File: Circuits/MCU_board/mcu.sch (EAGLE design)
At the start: 78 parts, among them IC1 RP111N331B-TR-FE, IC2 FT230XS, U1 TCA9548APWR, U2 USBLC6-2P6, U4 LSM9DS1, U5 STM32L452RECT6

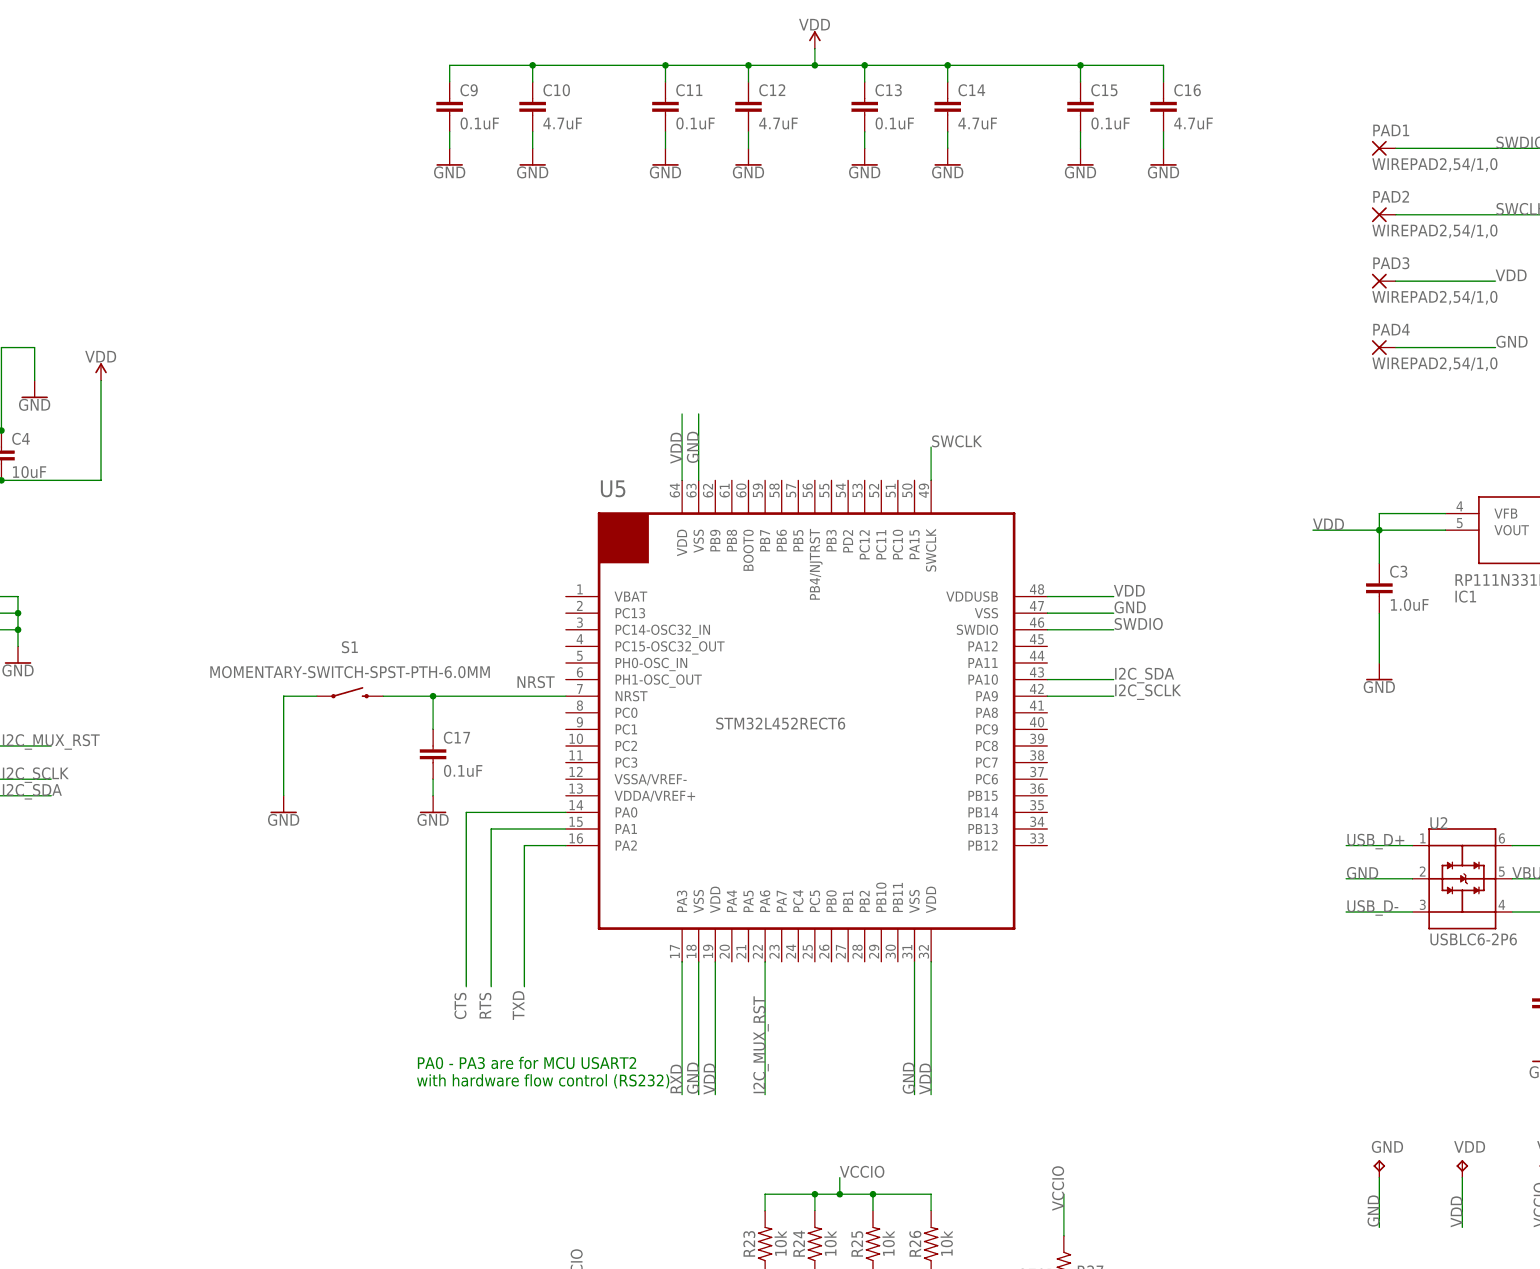
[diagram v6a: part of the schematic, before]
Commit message: Iteration 2 of MCU board * Change decoupling caps * Power all VDD and VSS pins * Add LED to GPIO * Add Pullup to USB D+ * Add jumpers for BOOT0
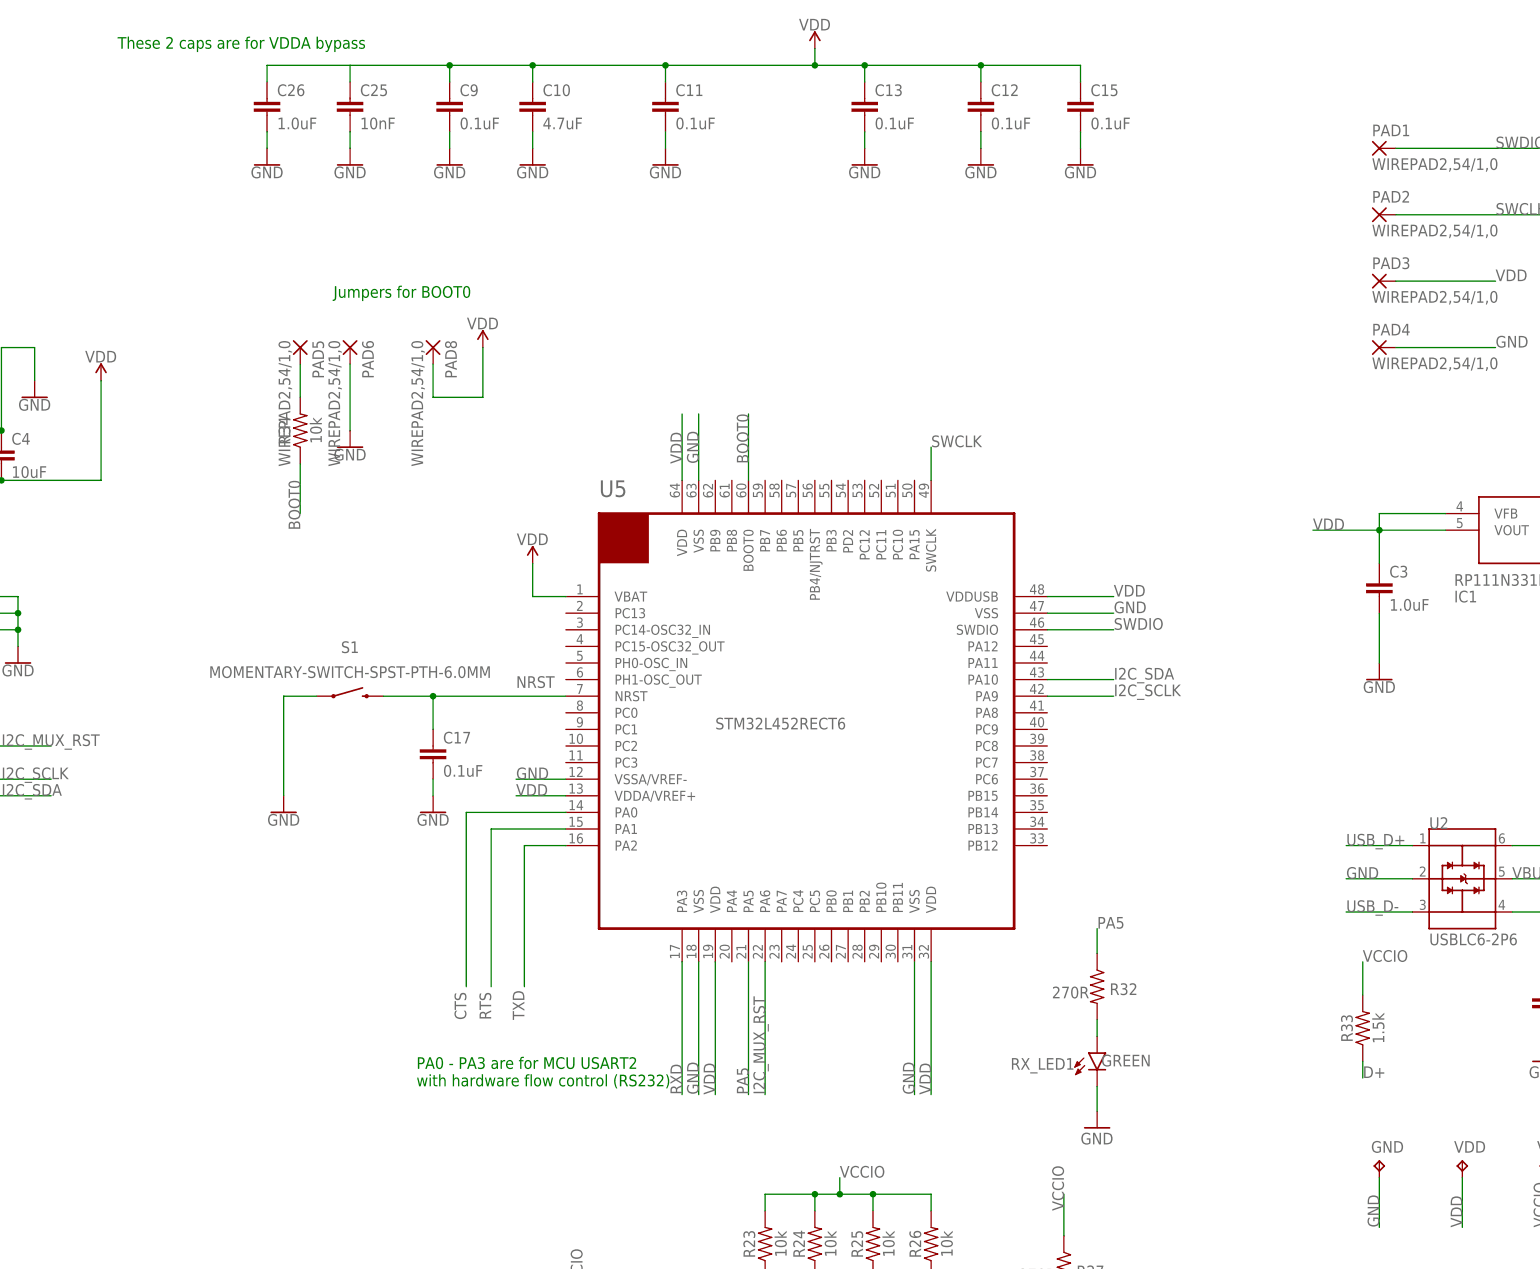
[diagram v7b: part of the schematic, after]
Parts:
- removed C14, C16: 4.7uF, SparkFun-Capacitors:4.7UF-0603-6.3V-(10%)
- added C25: 10nF, SparkFun-Capacitors:10NF-0603-50V-10%
- added C26: 1.0uF, SparkFun-Capacitors:1.0UF-0603-16V-10%-X7R
- added PAD5, PAD6, PAD8: WIREPAD2,54/1,0, wirepad:WIREPAD2,54/1,0
- added R32: 270R, SparkFun-Resistors:4.7KOHM-0603-1/10W-1%
- added R33: 1.5k, SparkFun-Resistors:1.5KOHM-0603-1/10W-1%
- added R34: 10k, SparkFun-Resistors:10KOHM-0603-1/10W-1%
- added RX_LED1: GREEN, SparkFun-LED:LED-GREEN0603
- C12: value 4.7uF -> 0.1uF; device SparkFun-Capacitors:4.7UF-0603-6.3V-(10%) -> SparkFun-Capacitors:0.1UF-0603-25V-(+80/-20%)
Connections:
- new net BOOT0: R34.1, U5.BOOT0
- new net N$19: R32.2, RX_LED1.A
- new net N$21: PAD5.P, R34.2
- new net PA5: R32.1, U5.PA5
- net D+: now also R33.1
- net GND: now also C25.2, C26.2, PAD6.P, RX_LED1.C, U5.VSSA/VREF-; no longer C14.2, C16.2
- net VCCIO: now also R33.2
- net VDD: now also C25.1, C26.1, PAD8.P, U5.VBAT, U5.VDDA/VREF+; no longer C14.1, C16.1
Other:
- note added: "Jumpers for BOOT0"
- note added: "These 2 caps are for VDDA bypass"
- moved on the sheet: C12

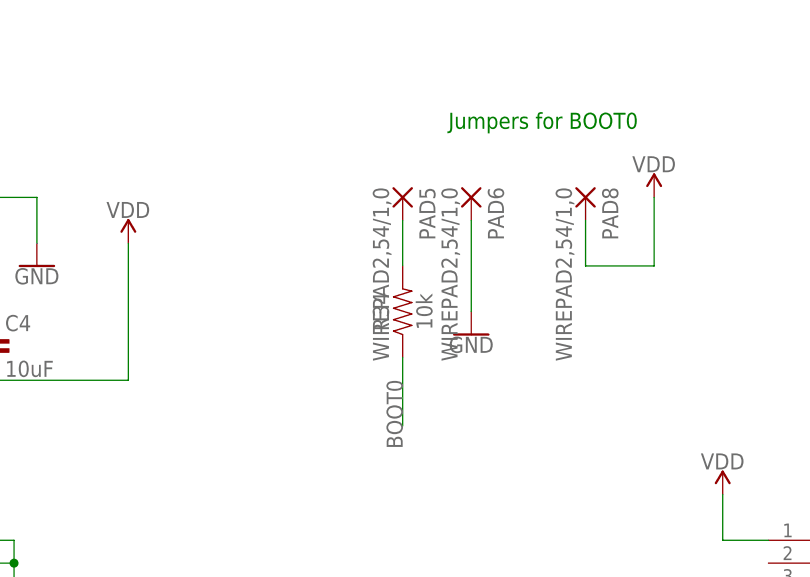
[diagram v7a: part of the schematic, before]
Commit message: Changed boot0 to testpad, routed all newly added components
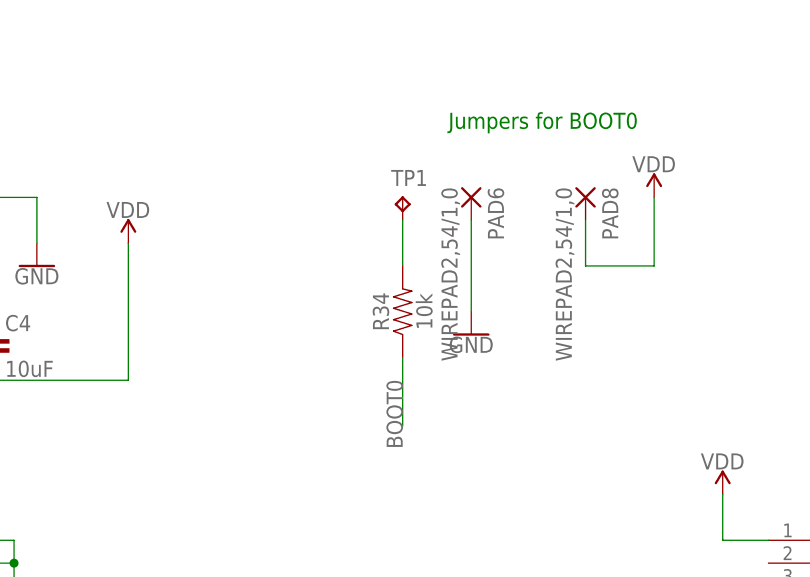
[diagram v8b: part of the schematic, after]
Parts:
- removed PAD5: WIREPAD2,54/1,0, wirepad:WIREPAD2,54/1,0
- added TP1: TPB1,27, testpad:TPB1,27
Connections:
- removed net N$21: PAD5.P, R34.2
- new net N$20: R34.2, TP1.TP
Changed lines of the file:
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@@
 <?xml version="1.0" encoding="utf-8"?>
 <!DOCTYPE eagle SYSTEM "eagle.dtd">
-<eagle version="9.3.2">
+<eagle version="9.4.2">
 <drawing>
 <settings>
@@
 <part name="R33" library="SparkFun-Resistors" deviceset="1.5KOHM" device="-0603-1/10W-1%" value="1.5k"/>
 <part name="GND21" library="supply1" library_urn="urn:adsk.eagle:library:371" deviceset="GND" device=""/>
-<part name="PAD5" library="wirepad" library_urn="urn:adsk.eagle:library:412" deviceset="WIREPAD" device="2,54/1,0" package3d_urn="urn:adsk.eagle:package:30828/1"/>
 <part name="PAD6" library="wirepad" library_urn="urn:adsk.eagle:library:412" deviceset="WIREPAD" device="2,54/1,0" package3d_urn="urn:adsk.eagle:package:30828/1"/>
 <part name="PAD8" library="wirepad" library_urn="urn:adsk.eagle:library:412" deviceset="WIREPAD" device="2,54/1,0" package3d_urn="urn:adsk.eagle:package:30828/1"/>
@@
 <part name="R34" library="SparkFun-Resistors" deviceset="10KOHM" device="-0603-1/10W-1%" value="10k"/>
 <part name="GND33" library="SparkFun-PowerSymbols" deviceset="GND" device=""/>
+<part name="TP1" library="testpad" library_urn="urn:adsk.eagle:library:385" deviceset="TP" device="B1,27" package3d_urn="urn:adsk.eagle:package:27944/2"/>
 </parts>
 <sheets>
@@
 <attribute name="VALUE" x="129.54" y="22.86" size="1.778" layer="96"/>
 </instance>
-<instance part="PAD5" gate="G$1" x="10.16" y="144.78" smashed="yes" rot="R270">
-<attribute name="NAME" x="12.0142" y="145.923" size="1.778" layer="95" rot="R270"/>
-<attribute name="VALUE" x="6.858" y="145.923" size="1.778" layer="96" rot="R270"/>
-</instance>
 <instance part="PAD6" gate="G$1" x="17.78" y="144.78" smashed="yes" rot="R270">
 <attribute name="NAME" x="19.6342" y="145.923" size="1.778" layer="95" rot="R270"/>
@@
 <instance part="GND33" gate="1" x="17.78" y="129.54" smashed="yes">
 <attribute name="VALUE" x="17.78" y="129.286" size="1.778" layer="96" align="top-center"/>
+</instance>
+<instance part="TP1" gate="G$1" x="10.16" y="144.78" smashed="yes">
+<attribute name="NAME" x="8.89" y="146.05" size="1.778" layer="95"/>
+<attribute name="TP_SIGNAL_NAME" x="11.43" y="143.51" size="1.778" layer="97"/>
 </instance>
 </instances>
@@
 </segment>
 </net>
-<net name="N$21" class="0">
-<segment>
+<net name="N$20" class="0">
+<segment>
+<pinref part="TP1" gate="G$1" pin="TP"/>
 <pinref part="R34" gate="G$1" pin="2"/>
-<pinref part="PAD5" gate="G$1" pin="P"/>
-<wire x1="10.16" y1="137.16" x2="10.16" y2="142.24" width="0.1524" layer="91"/>
-</segment>
-</net>
+<wire x1="10.16" y1="142.24" x2="10.16" y2="137.16" width="0.1524" layer="91"/>
+</segment>
+</net>
